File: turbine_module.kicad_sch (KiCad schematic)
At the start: 12 parts, among them M3 Motor_Servo, M4 LP-MSPM0G3507

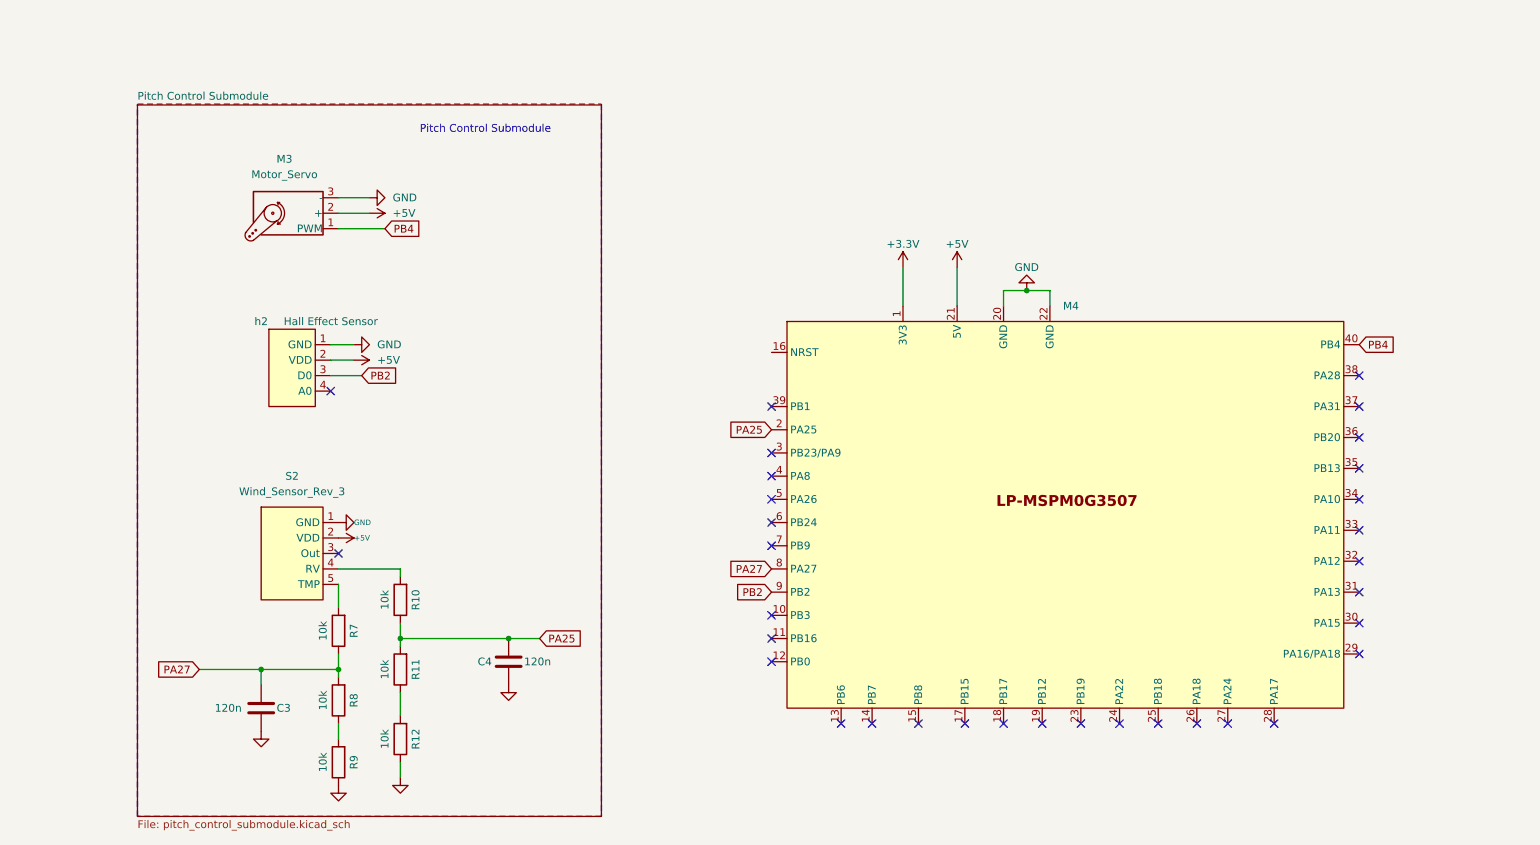
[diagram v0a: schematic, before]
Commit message: Finished Squematics V1
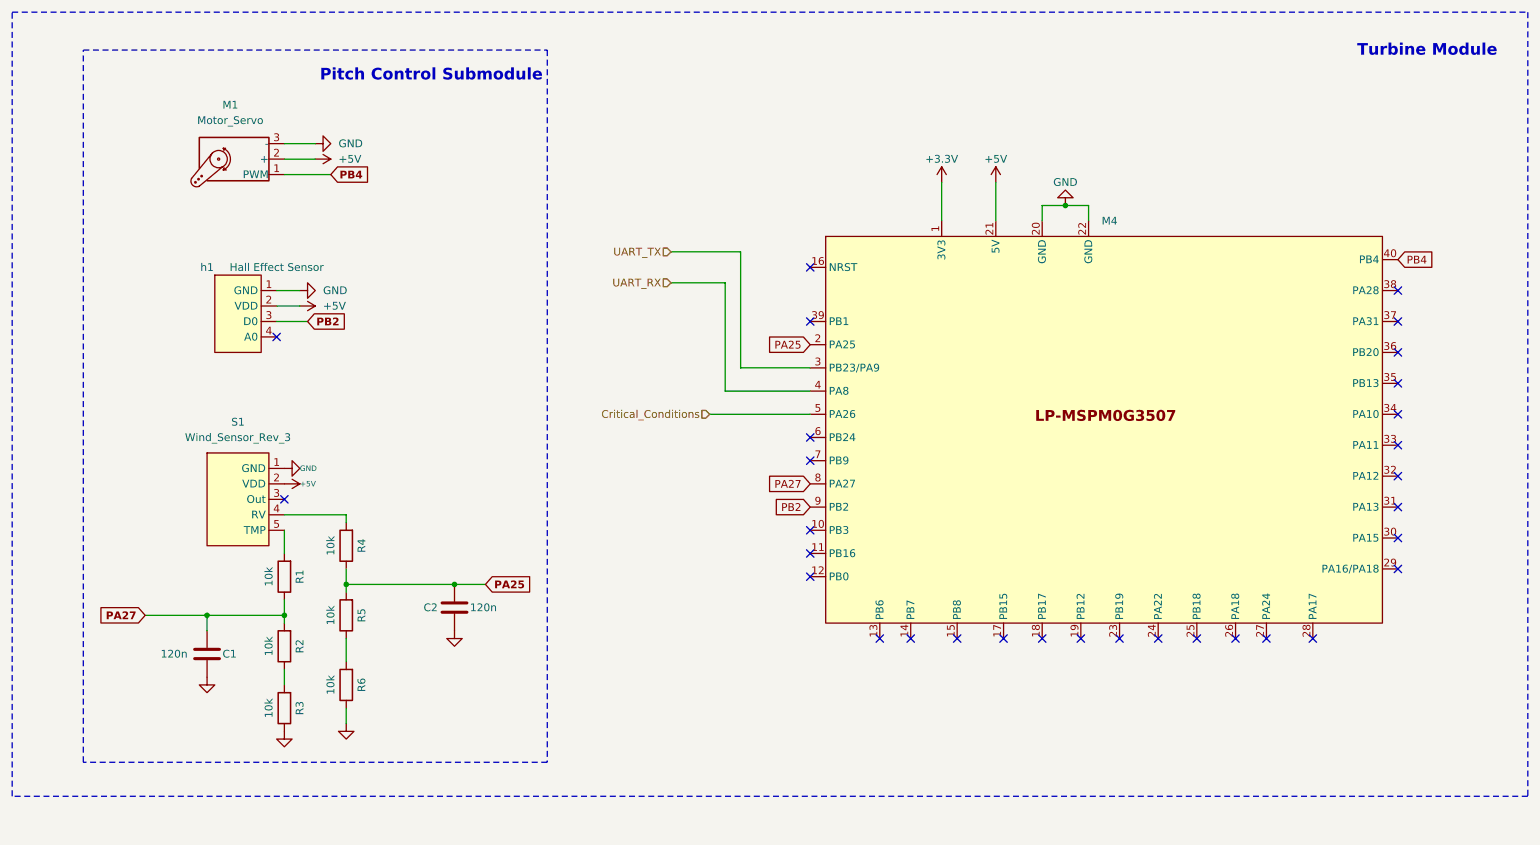
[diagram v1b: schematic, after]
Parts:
- removed C3, C4: 120n, symbol Device:C
- removed M3: Motor_Servo, symbol Motor:Motor_Servo
- removed R10, R11, R12, R7, R8, R9: 10k, symbol Device:R
- removed S2: Wind_Sensor_Rev_3, symbol windTurbineSchemSymLib:Wind_Sensor_Rev_C
- removed h2: Hall Effect Sensor, symbol windTurbineSchemSymLib:hall_effect_sensor
- added C1, C2: 120n, symbol Device:C
- added M1: Motor_Servo, symbol Motor:Motor_Servo
- added R1, R2, R3, R4, R5, R6: 10k, symbol Device:R
- added S1: Wind_Sensor_Rev_3, symbol windTurbineSchemSymLib:Wind_Sensor_Rev_C
- added h1: Hall Effect Sensor, symbol windTurbineSchemSymLib:hall_effect_sensor
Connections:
- net +5V: now also M1.2 (+), S1.2 (VDD), h1.2 (VDD)
- net GND: now also C1.2, C2.2, M1.3 (-), R3.1, R6.1, S1.1 (GND), h1.1 (GND)
- net PA25: now also C2.1, R4.1, R5.2
- net PA27: now also C1.1, R1.1, R2.2
- net PB2: now also h1.3 (D0)
- net PB4: now also M1.1 (PWM)
- net UART_TX: now reaches M4.3 (PB23/PA9)
- net UART_RX: now reaches M4.4 (PA8)
- net Critical_Conditions: now reaches M4.5 (PA26)
- new net: R2.1, R3.2
- new net: R5.1, R6.2
- new net: R1.2, S1.5 (TMP)
- new net: R4.2, S1.4 (RV)
- no-connect marks 33 -> 31
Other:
- removed sheet Pitch Control Submodule
- note added: "Turbine Module"
- company: (none) -> PRES
- title: (none) -> Turbine Module
- moved on the sheet: M4

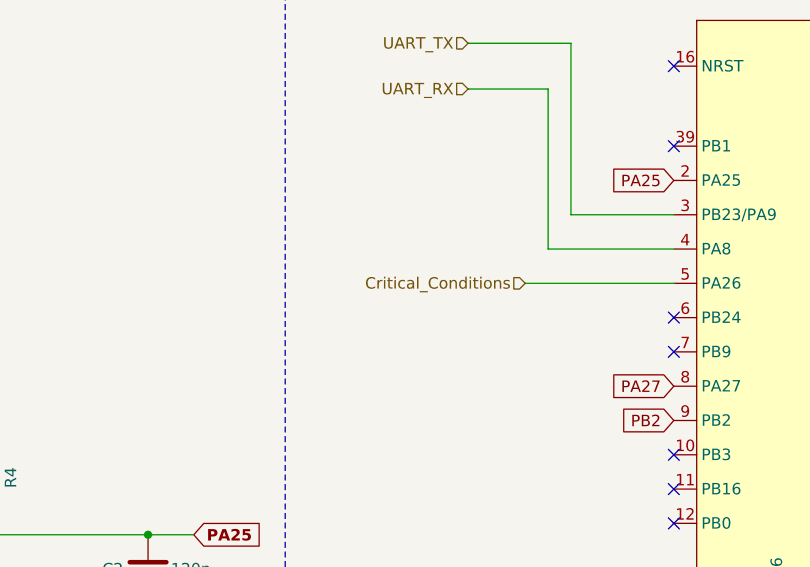
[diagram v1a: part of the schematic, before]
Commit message: Changed a wire name
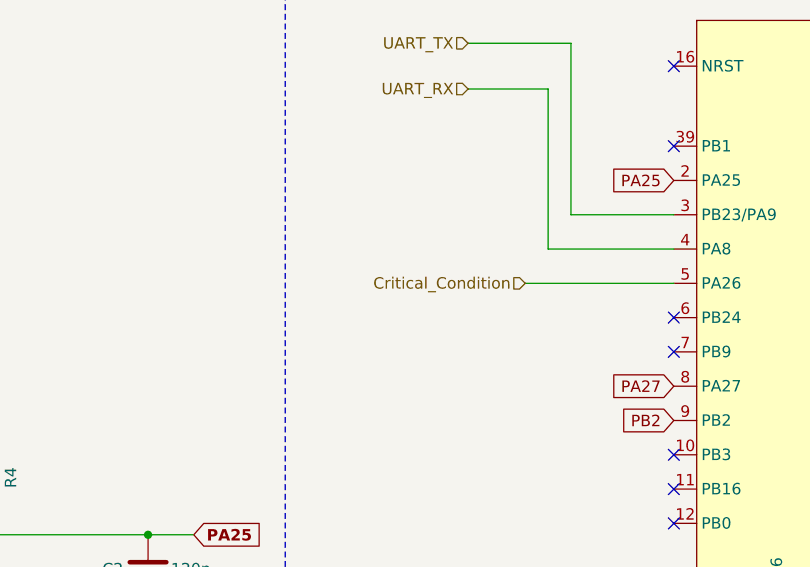
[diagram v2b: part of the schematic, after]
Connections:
- net Critical_Conditions renamed Critical_Condition
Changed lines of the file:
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@@
 		)
 	)
-	(hierarchical_label "Critical_Conditions"
+	(hierarchical_label "Critical_Condition"
 		(shape input)
 		(at 143.51 92.71 180)
